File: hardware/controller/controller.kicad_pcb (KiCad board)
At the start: 2 copper layers, 30 x 100 mm, 35 parts, among them J1 DC_12V_IN, J2 HDD_POWER_OUT, J3 470531000, J4 470531000, J5 Conn_01x07, Q1 2N3904, Q2 2N3904, U1 TSR0.5-2450, U2 XIAO-RP2350-SMD, U3 INA228, U4 74HC4051

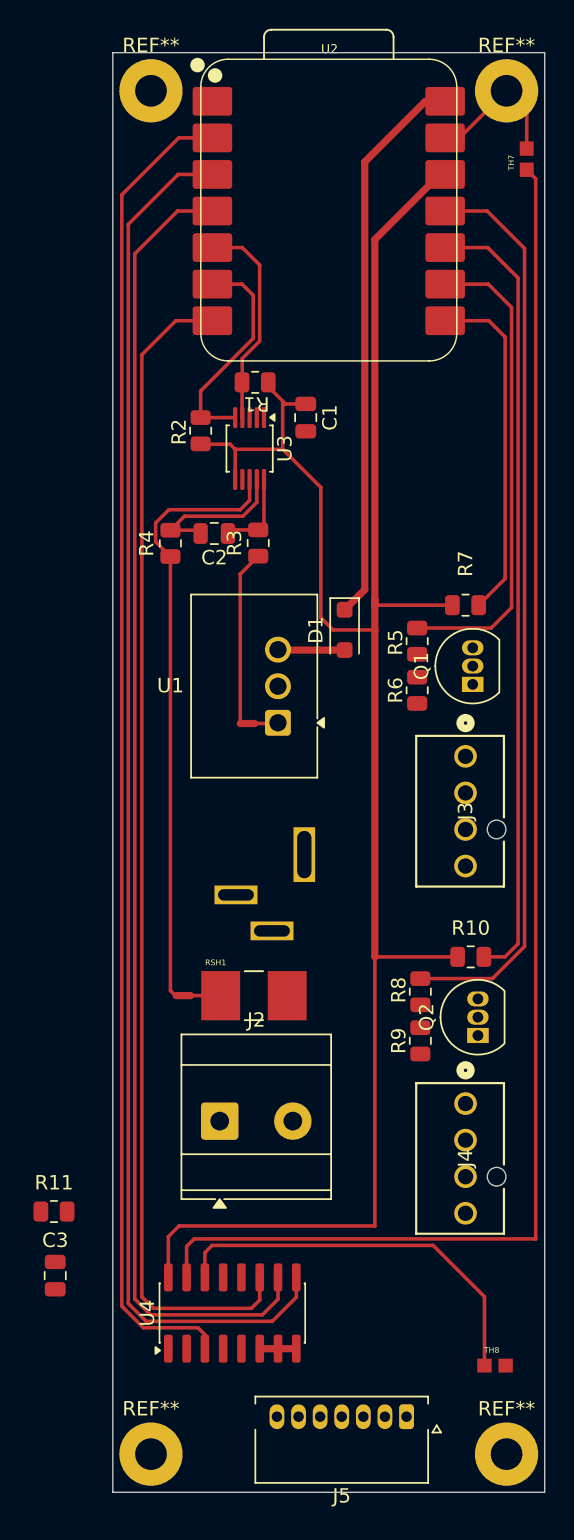
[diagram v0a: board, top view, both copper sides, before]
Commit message: First complete pass of routing for controller + DRC report
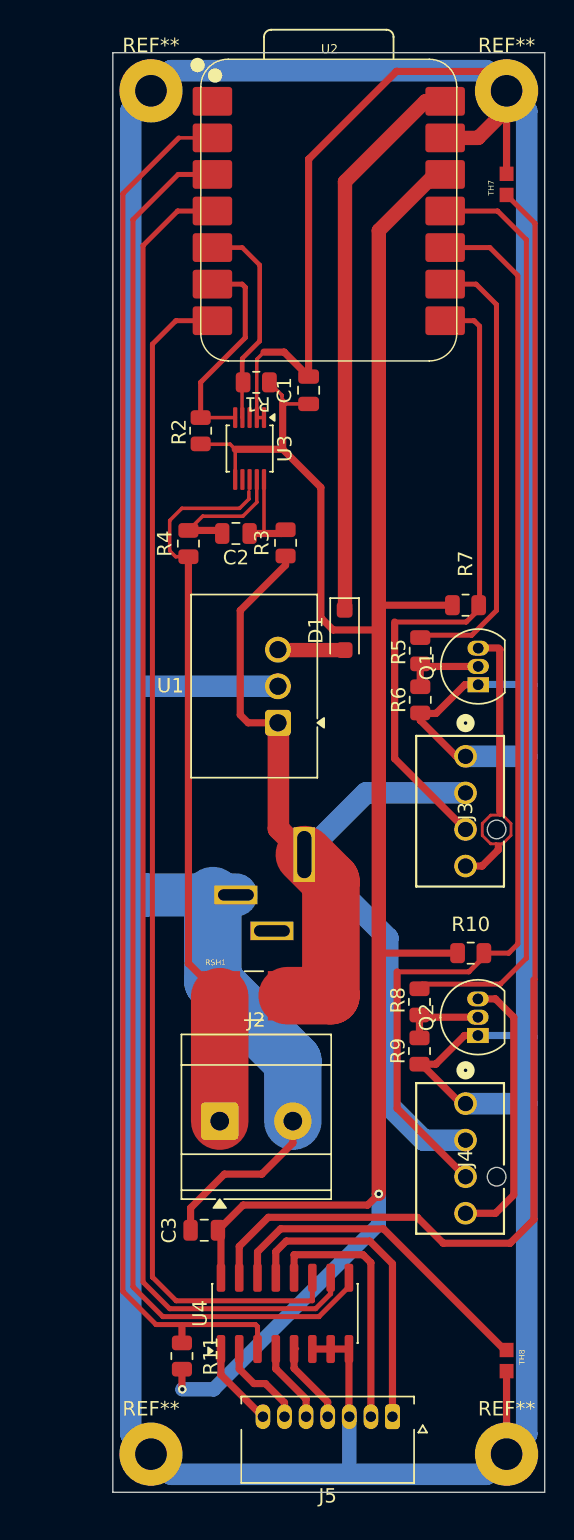
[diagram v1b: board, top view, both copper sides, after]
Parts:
- removed NT1, NT2: NetTie_2, NetTie:NetTie-2_SMD_Pad0.5mm
- moved R11 13.4 mm to (55.3, 139.5), turned to 90 degrees
- moved C3 10.8 mm to (56.9, 130.8), turned to 180 degrees
- moved U4 3.66 mm to (62.5, 136.6)
- moved TH7 2.24 mm to (77.8, 58.1)
- moved C1 1.91 mm to (64.1, 72.5), turned to 90 degrees
- moved R3 1.90 mm to (62.5, 83.0)
- moved C2 1.50 mm to (59.0, 82.4)
- moved R4 1.25 mm to (55.8, 83.1)
- moved J5 0.98 mm to (69.9, 143.8)
- moved TH8 0.87 mm to (77.8, 139.8), turned to -90 degrees
- moved R8 0.71 mm to (71.8, 114.9)
- moved R9 0.71 mm to (71.8, 118.3)
- moved R5 0.70 mm to (71.9, 90.5)
- moved R6 0.70 mm to (71.9, 94.0)
- moved Q1 0.38 mm to (75.9, 92.9)
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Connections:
- J5 pad 1: /TH1 -> /TH6
- J5 pad 2: /TH2 -> /TH5
- J5 pad 3: /TH3 -> GND
- J5 pad 5: GND -> /TH3
- J5 pad 6: /TH5 -> /TH2
- J5 pad 7: /TH6 -> /TH1
- R3 pad 1: /12V_IN_SENSE -> /12V_IN
- R4 pad 1: /12V_HDD_SENSE -> /12V_HDD
- U3 pad 8: /12V_HDD_SENSE -> /12V_HDD
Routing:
- net GND: track 13.9 -> 398.9 mm
- net /12V_IN: track 1.49 -> 77.9 mm
- net /12V_HDD: track 2.14 -> 52.4 mm
- net /12V_HDD_SENSE: track 42.0 -> 0.00 mm
- net Net-(Q1-C): track 0.00 -> 22.9 mm
- net /FAN2_TACH: track 54.9 -> 77.7 mm
- net /TH6: track 0.00 -> 21.5 mm
- net /FAN1_TACH: track 24.0 -> 44.9 mm
- net Net-(Q2-C): track 0.00 -> 19.2 mm
- net /TH5: track 0.00 -> 17.9 mm
- net +3.3V: track 136.0 -> 152.8 mm, vias 0 -> 2
- net /12V_IN_SENSE: track 12.1 -> 0.00 mm
- net /TH2: track 0.00 -> 6.47 mm
- net /TH1: track 0.00 -> 5.91 mm
- net /TH4: track 0.00 -> 5.75 mm
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
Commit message: various fixes for DRC
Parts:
- moved REF** 0.07 mm to (53.2, 51.7)
- moved REF** 0.07 mm to (77.8, 51.7)
- moved REF** 0.07 mm to (53.2, 146.3)
- moved REF** 0.07 mm to (77.8, 146.3)
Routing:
- net GND: track 398.9 -> 421.4 mm
- net /12V_HDD: track 52.4 -> 51.3 mm
